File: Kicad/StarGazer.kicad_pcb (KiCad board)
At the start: 4 copper layers, 99.9 x 99.9 mm, 108 parts, among them J201 USB_B_Micro, J202 JST - 2x1, J203 Conn_01x01, J204 Conn_01x01, J301 JST - 4x1, J302 JST - 4x1, J303 JST - 5x1, J304 JST - 5x1, SW201 JST - 2x1, SW301 RESET PUSH, U101 STM32G070KBT6, U201 STBC08, U202 AP22811BW5-7, U203 TLV75528PDBVR, U301 TSX-3225, U302 MMC5603NJ, U303 LSM6DS33TR, U304 74HC595PW,112, U305 74HC595PW,112, U306 74HC595PW,112

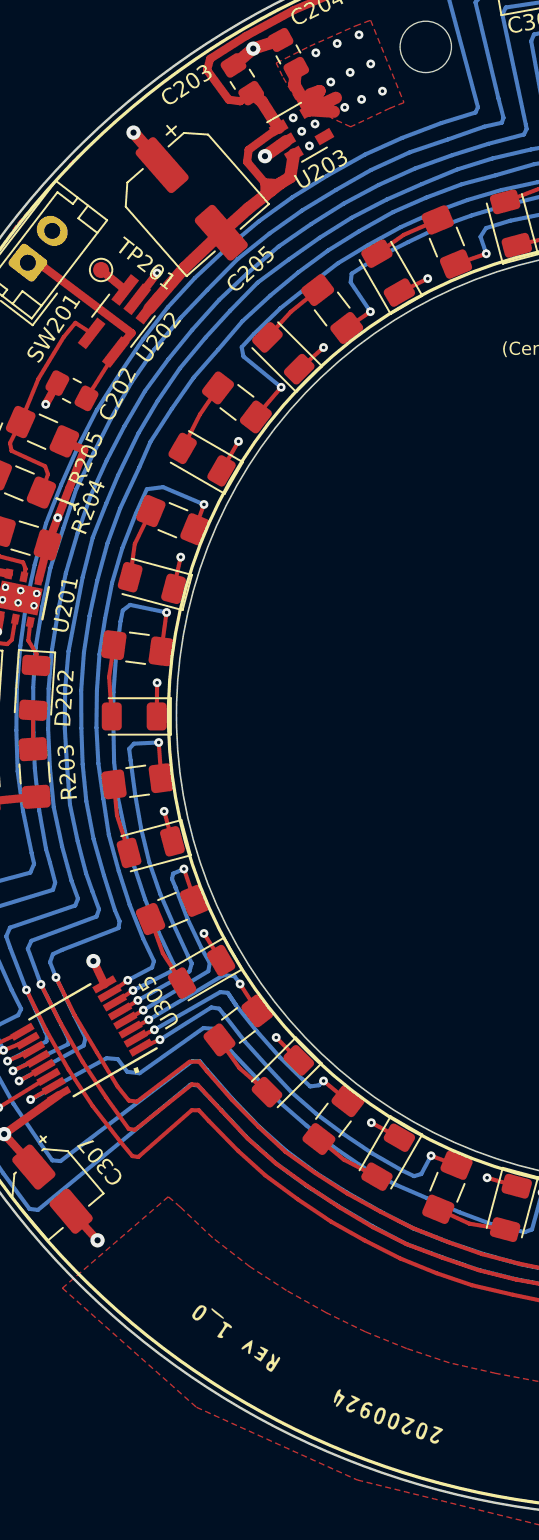
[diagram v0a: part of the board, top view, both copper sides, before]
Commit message: Added images.  Small schematic corrections
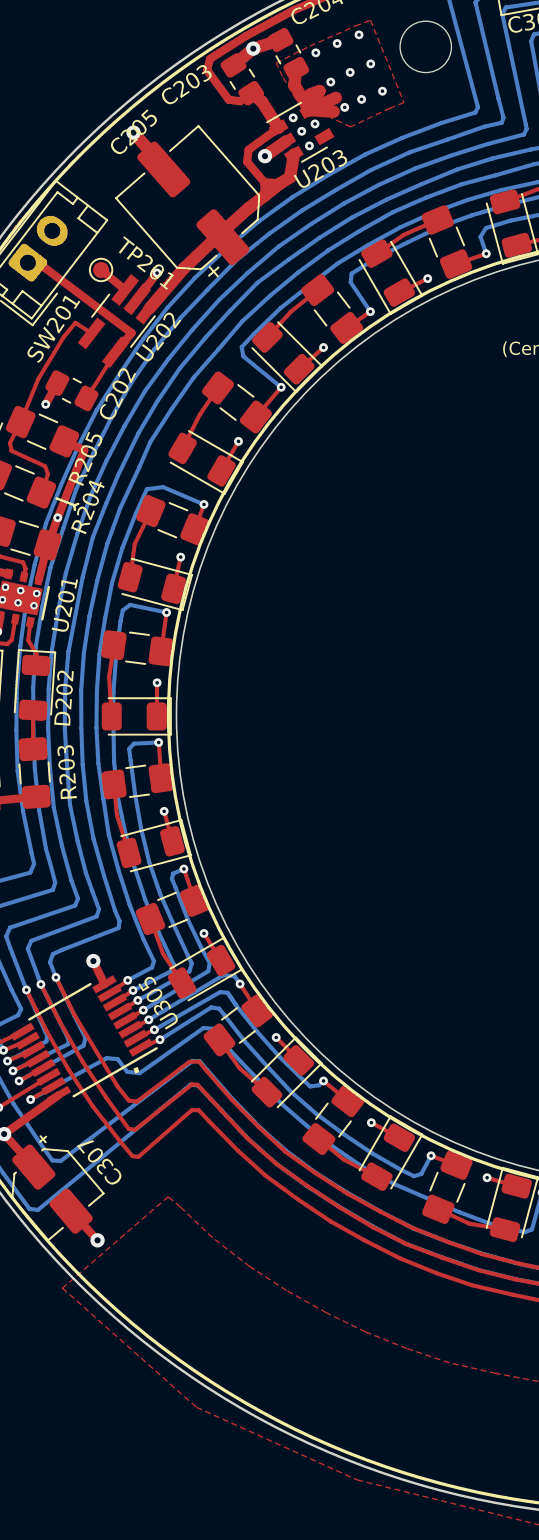
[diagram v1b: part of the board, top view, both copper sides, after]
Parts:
- removed G***: LOGO, Kicad:Label_URL
- removed G***: LOGO, Kicad:Label_Name
- removed G***: LOGO, Kicad:Label_Date_Rev
- removed G***: LOGO, Kicad:Back_Art
- moved C205 0.29 mm to (131.9, 58.0), turned to 131.2 degrees
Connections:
- C205 pad 1: GND -> SW_3_3V
- C205 pad 2: SW_3_3V -> GND
- U201 pad 7: GND -> (no net)
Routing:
- net GND: vias 53 -> 47
- net (no net): vias 13 -> 19
